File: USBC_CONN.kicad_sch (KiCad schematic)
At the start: 5 parts, among them J1 USB_C_Receptacle, J2 USB_C_Receptacle, U2 TPS2560

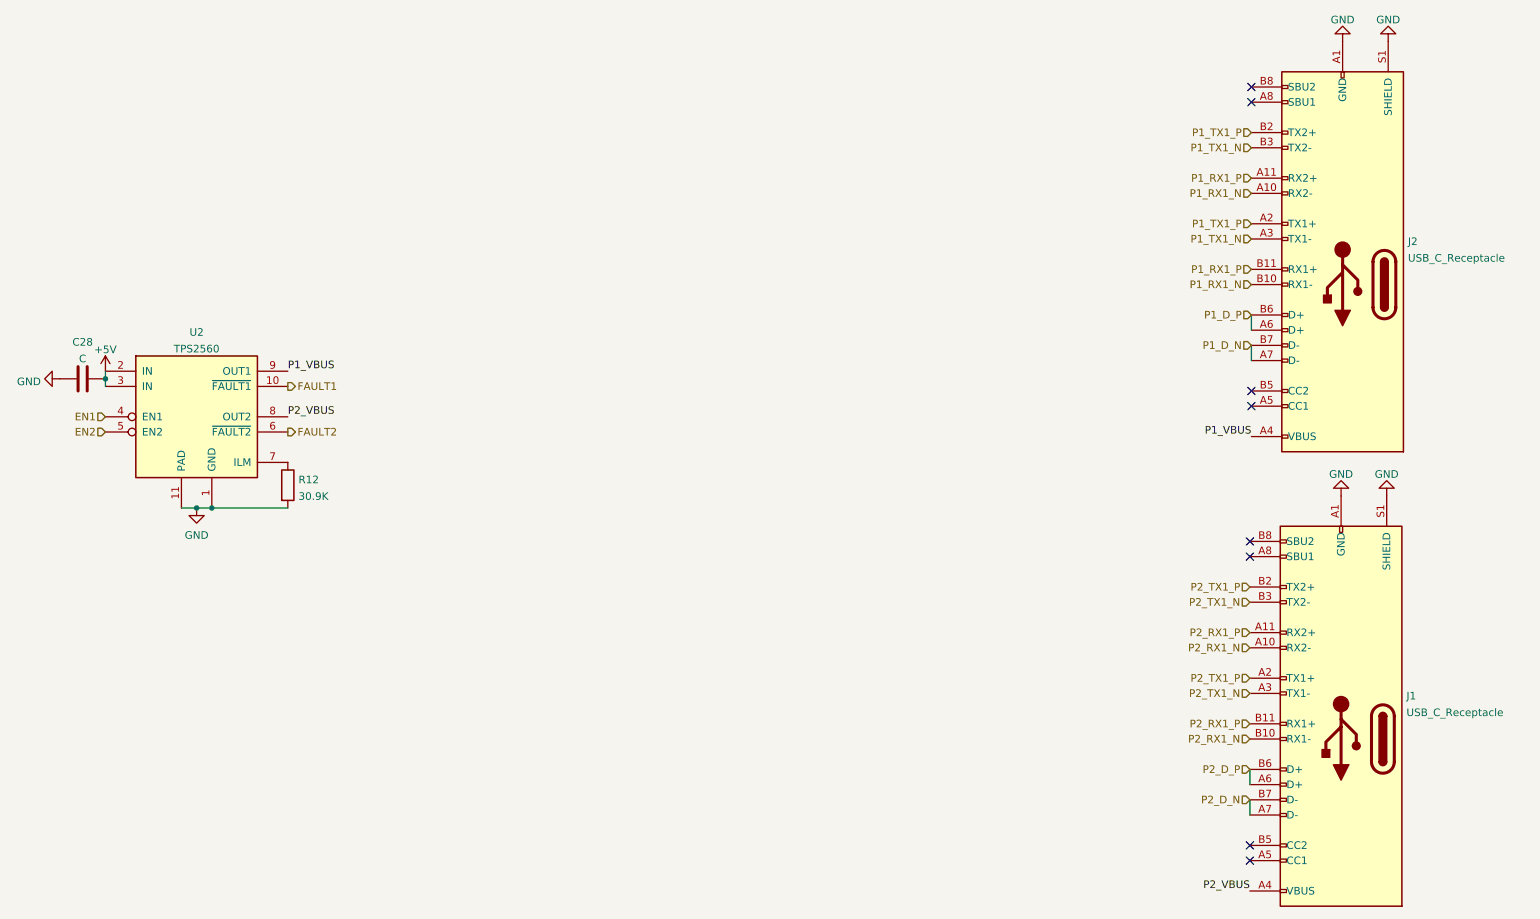
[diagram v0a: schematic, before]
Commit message: Initial layout and all parts added. Some pins still not connected to power
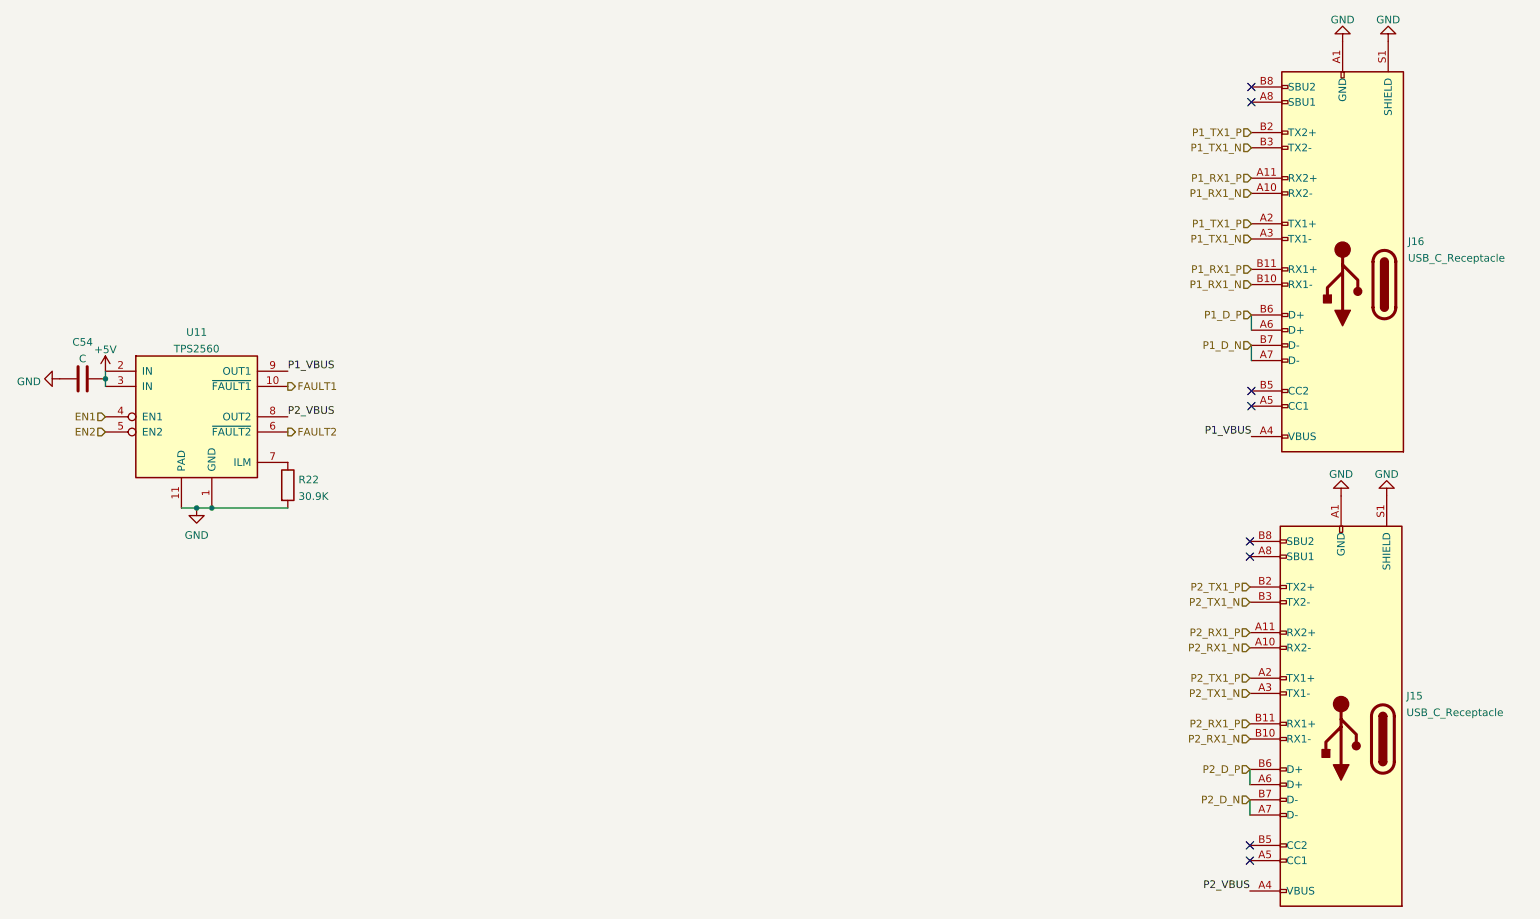
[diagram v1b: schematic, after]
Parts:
- renumbered C28 to C54, J1 to J15, J2 to J16, R12 to R22, U2 to U11

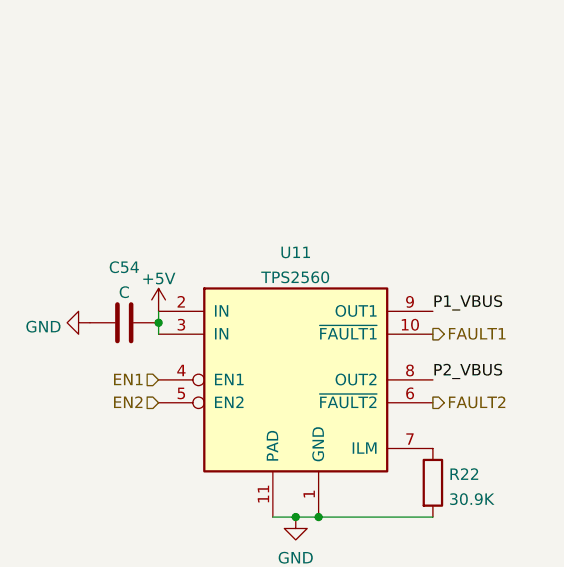
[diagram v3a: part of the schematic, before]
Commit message: Added usb to ethernet and changed mcu to stm32g4
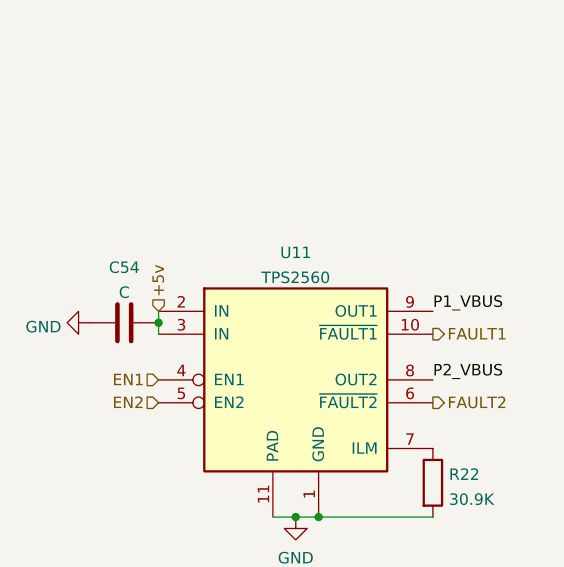
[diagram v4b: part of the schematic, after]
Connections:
- net +5V renamed +5v
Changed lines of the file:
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@@
 (kicad_sch (version 20210621) (generator eeschema)
   (paper "A4")
+  (junction (at 69.342 98.298) (diameter 0) (color 0 0 0 0))
+  (junction (at 66.802 98.298) (diameter 0) (color 0 0 0 0))
   (junction (at 51.562 76.708) (diameter 0) (color 0 0 0 0))
-  (junction (at 66.802 98.298) (diameter 0) (color 0 0 0 0))
-  (junction (at 69.342 98.298) (diameter 0) (color 0 0 0 0))
   (no_connect (at 242.824 106.426))
   (no_connect (at 242.824 157.226))
@@
     (effects (font (size 1.27 1.27)) (justify right))
   )
+  (hierarchical_label "+5v" (shape input) (at 51.562 75.438 90)
+    (effects (font (size 1.27 1.27)) (justify left))
+  )
   (hierarchical_label "P1_TX1_N" (shape input) (at 243.078 38.1 180)
     (effects (font (size 1.27 1.27)) (justify right))
@@
       (effects (font (size 1.27 1.27)) hide)
     )
-    (pin "1")
-  )
-  (symbol (lib_id "power:+5V") (at 51.562 75.438 0) (unit 1)
-    (in_bom yes) (on_board yes) (fields_autoplaced)
-    (property "Reference" "#PWR061" (id 0) (at 51.562 79.248 0)
-      (effects (font (size 1.27 1.27)) hide)
-    )
-    (property "Value" "+5V" (id 1) (at 51.562 71.8335 0))
-    (property "Footprint" "" (id 2) (at 51.562 75.438 0)
-      (effects (font (size 1.27 1.27)) hide)
-    )
-    (property "Datasheet" "" (id 3) (at 51.562 75.438 0)
-      (effects (font (size 1.27 1.27)) hide)
-    )
